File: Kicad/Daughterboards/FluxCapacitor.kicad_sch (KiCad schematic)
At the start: 28 parts, among them J10 RELAY, J19 JST_PH_01x03_Socket, J20 JST_PH_01x03_Socket, J21 JST_PH_01x03_Socket, J22 JST_PH_01x03_Socket, J23 JST_PH_01x03_Socket, J4 TREADMILL_CTRL_PANEL1, K1 G5V-1, Q1 2N7000, SW1 SW_SPDT_321, SW9 SW_Push_Open_Dual, U6 SMF5.0A-T13

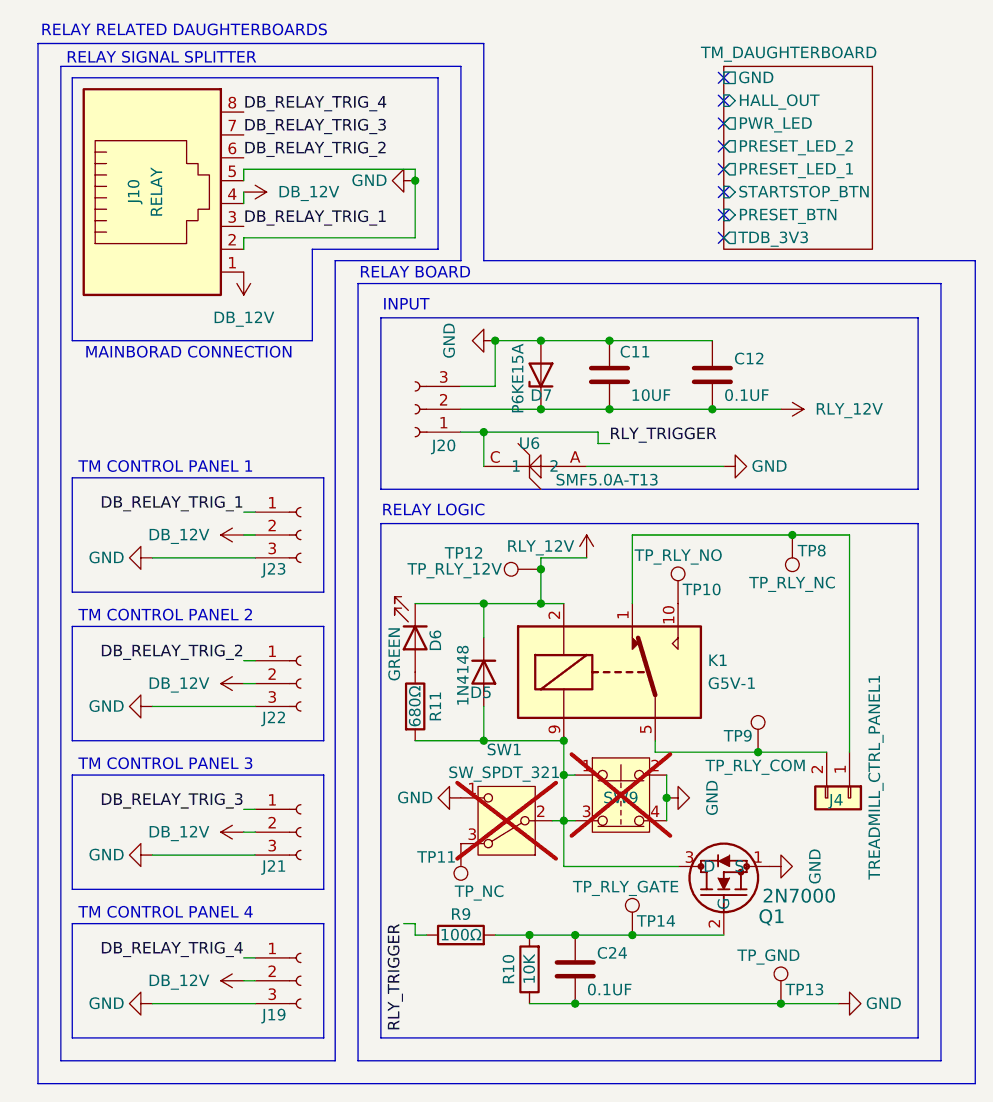
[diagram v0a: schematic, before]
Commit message: Finished project
Made daughterboard pcbs, fixed silkscreen errors on mainboard pcb, generated GERBERs and drill files
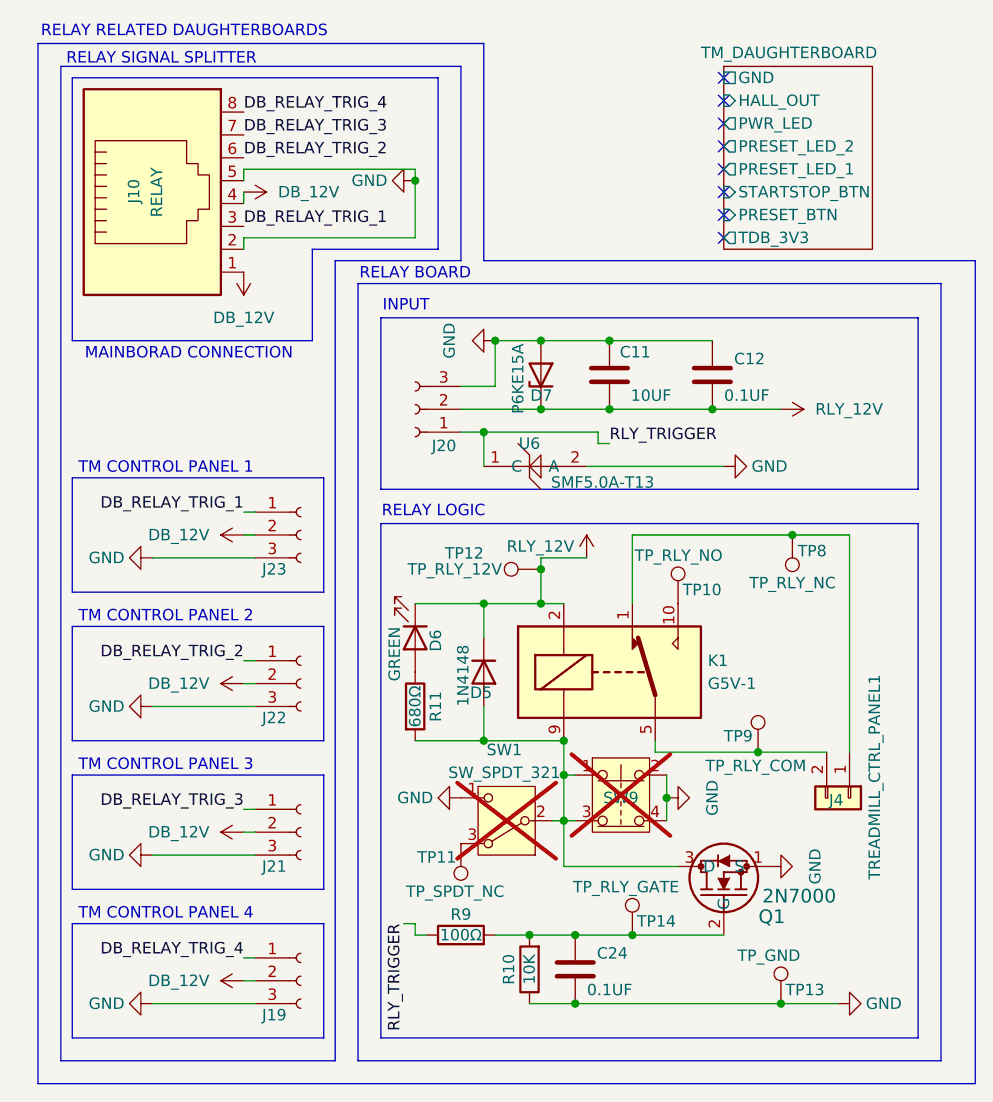
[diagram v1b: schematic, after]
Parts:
- TP11: value TP_NC -> TP_SPDT_NC
- U6: footprint FluxCapacitor:SMF5.0A-T13 -> (none)
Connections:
- net GND: now also U6.2 (A); no longer U6.A (2)
- net RLY_TRIGGER: now also U6.1 (C); no longer U6.C (1)
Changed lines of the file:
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@@
 	)
 	(junction
-		(at 227.33 90.17)
-		(diameter 0)
-		(color 0 0 0 0)
-	)
-	(junction
 		(at 241.3 87.63)
 		(diameter 0)
@@
 	)
 	(junction
+		(at 227.33 90.17)
+		(diameter 0)
+		(color 0 0 0 0)
+	)
+	(junction
 		(at 233.68 105.41)
 		(diameter 0)
@@
 		)
 		(property "Value" "SMF5.0A-T13"
-			(at 241.046 95.504 0)
+			(at 240.538 95.758 0)
 			(show_name no)
 			(do_not_autoplace no)
@@
 			)
 		)
-		(property "Footprint" "FluxCapacitor:SMF5.0A-T13"
+		(property "Footprint" ""
 			(at 232.41 93.98 0)
 			(hide yes)
@@
 			)
 		)
-		(pin "C"
+		(pin "1"
 		)
-		(pin "A"
+		(pin "2"
 		)
 		(instances
@@
 			)
 		)
-		(property "Value" "TP_NC"
+		(property "Value" "TP_SPDT_NC"
 			(at 229.616 141.224 0)
 			(show_name no)
